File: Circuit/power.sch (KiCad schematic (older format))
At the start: 20 parts, among them Q202 FDN340P, Q203 FDN340P, SW1 ON/OFF, U201 CN3063, U202 MCP6002, U3 LXDC2XQ

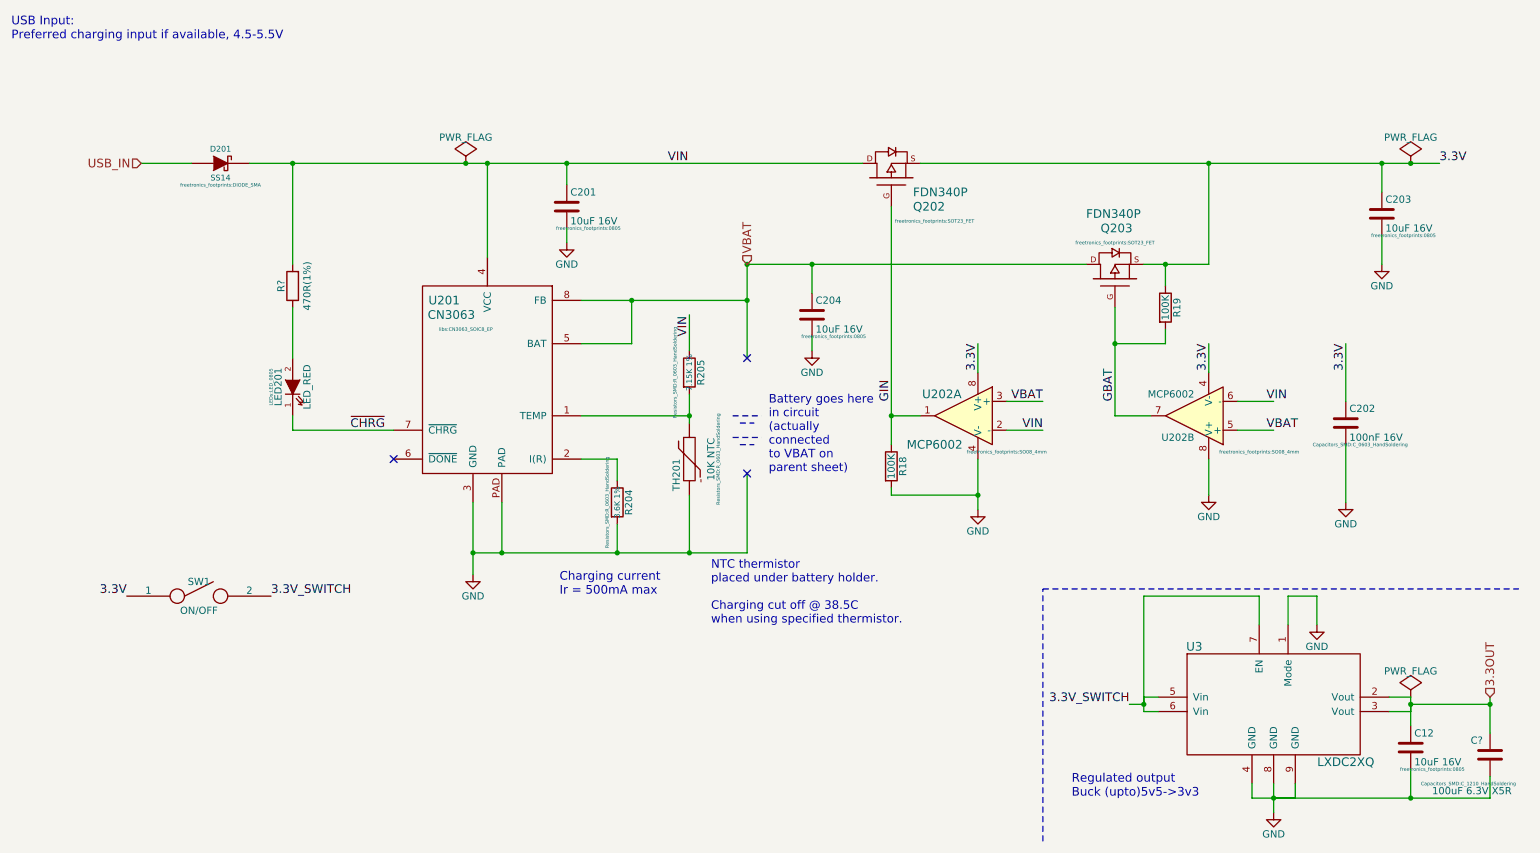
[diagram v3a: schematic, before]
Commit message: Adding LED to 3v3 line.
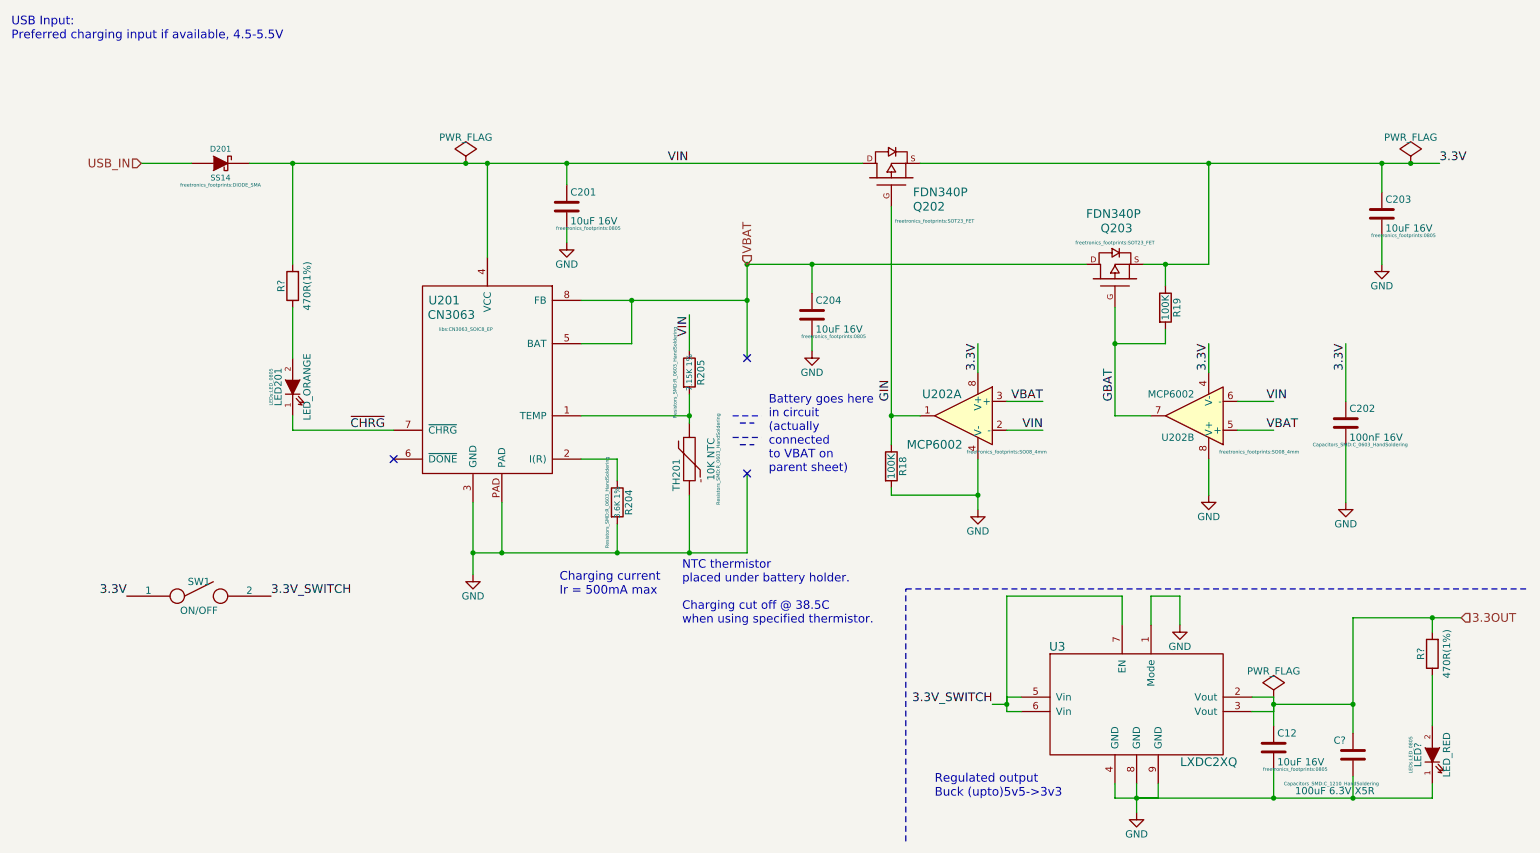
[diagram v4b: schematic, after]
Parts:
- added LED?: LED_RED, LEDs:LED_0805, symbol LED
- added R?: 470R(1%), Resistors_SMD:R_0603_HandSoldering, symbol R
- LED201: value LED_RED -> LED_ORANGE; Digikey PN (none) -> 160-1413-1-ND; Link (none) -> http://www.digikey.com.au/product-detail/en/lite-on-inc/LTS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; Manufacturer PN (none) -> LTST-C170KFKT; Unit Cost (none) -> 0.31
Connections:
- wire segments 74 -> 78
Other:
- moved on the sheet: C12, C?, U3
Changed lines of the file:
@@
 P 2700 3350
 F 0 "LED201" H 2700 3450 50  0000 C CNN
-F 1 "LED_RED" H 2700 3250 50  0000 C CNN
+F 1 "LED_ORANGE" H 2700 3250 50  0000 C CNN
 F 2 "LEDs:LED_0805" H 2700 3500 24  0000 C CNN
 F 3 "" H 2700 3350 60  0000 C CNN
+F 4 "160-1413-1-ND" H 2700 3350 60  0001 C CNN "Digikey PN"
+F 5 "http://www.digikey.com.au/product-detail/en/lite-on-inc/LTST-C170KFKT/160-1413-1-ND/386774" H 2700 3350 60  0001 C CNN "Link"
+F 6 "LTST-C170KFKT" H 2700 3350 60  0001 C CNN "Manufacturer PN"
+F 7 "0.31" H 2700 3350 60  0001 C CNN "Unit Cost"
 	1    2700 3350
 	0    -1   -1   0
@@
 Text Label 6850 3450 1    60   ~ 0
 GIN
-Text HLabel 11000 5500 1    60   Input ~ 0
+Text HLabel 10800 4950 2    60   Input ~ 0
 3.3OUT
 $Comp
@@
 L C C?
 U 1 1 5642CCBE
-P 11000 5900
-F 0 "C?" H 11050 5800 50  0000 L CNN
-F 1 "100uF 6.3V X5R" H 10850 6150 50  0000 L CNN
-F 2 "Capacitors_SMD:C_1210_HandSoldering" H 11150 6100 24  0000 C CNN
-F 3 "" H 11000 5900 60  0000 C CNN
-F 4 "490-7217-1-ND" H 11000 5900 60  0001 C CNN "Digikey PN"
-F 5 "http://www.digikey.com.au/product-detail/en/murata-electronics-north-america/GRM31CR60J107ME39K/490-7217-1-ND/3991203" H 11000 5900 60  0001 C CNN "Link"
-F 6 "GRM31CR60J107ME39K" H 11000 5900 60  0001 C CNN "Manufacturer PN"
-F 7 "0.60" H 11000 5900 60  0001 C CNN "Unit Cost"
-	1    11000 5900
+P 10050 5900
+F 0 "C?" H 10100 5800 50  0000 L CNN
+F 1 "100uF 6.3V X5R" H 9900 6150 50  0000 L CNN
+F 2 "Capacitors_SMD:C_1210_HandSoldering" H 10200 6100 24  0000 C CNN
+F 3 "" H 10050 5900 60  0000 C CNN
+F 4 "490-7217-1-ND" H 10050 5900 60  0001 C CNN "Digikey PN"
+F 5 "http://www.digikey.com.au/product-detail/en/murata-electronics-north-america/GRM31CR60J107ME39K/490-7217-1-ND/3991203" H 10050 5900 60  0001 C CNN "Link"
+F 6 "GRM31CR60J107ME39K" H 10050 5900 60  0001 C CNN "Manufacturer PN"
+F 7 "0.60" H 10050 5900 60  0001 C CNN "Unit Cost"
+	1    10050 5900
 	-1   0    0    1
 $EndComp
@@
 Text Label 5450 3000 1    60   ~ 0
 VIN
-Text Notes 5600 5000 0    59   ~ 0
+Text Notes 5400 5000 0    59   ~ 0
 NTC thermistor\nplaced under battery holder.\n\nCharging cut off @ 38.5C\nwhen using specified thermistor.
 $Comp
@@
 Text Label 10650 1800 0    60   ~ 0
 3.3V
-Text Label 8500 5550 2    60   ~ 0
+Text Label 7550 5550 2    60   ~ 0
 3.3V_SWITCH
 Text Label 2550 4800 0    60   ~ 0
@@
 Text Label 1550 4800 2    60   ~ 0
 3.3V
-Text Notes 8100 6200 0    60   ~ 0
+Text Notes 7150 6200 0    60   ~ 0
 Regulated output\nBuck (upto)5v5->3v3
 Text Label 7450 3050 3    60   ~ 0
@@
 L GND #PWR040
 U 1 1 5812C93A
-P 9500 6300
-F 0 "#PWR040" H 9500 6050 50  0001 C CNN
-F 1 "GND" H 9500 6150 50  0000 C CNN
-F 2 "" H 9500 6300 60  0000 C CNN
-F 3 "" H 9500 6300 60  0000 C CNN
-	1    9500 6300
+P 8550 6300
+F 0 "#PWR040" H 8550 6050 50  0001 C CNN
+F 1 "GND" H 8550 6150 50  0000 C CNN
+F 2 "" H 8550 6300 60  0000 C CNN
+F 3 "" H 8550 6300 60  0000 C CNN
+	1    8550 6300
 	1    0    0    -1
 $EndComp
@@
 L GND #PWR041
 U 1 1 5812E212
-P 9800 5000
-F 0 "#PWR041" H 9800 4750 50  0001 C CNN
-F 1 "GND" H 9800 4850 50  0000 C CNN
-F 2 "" H 9800 5000 60  0000 C CNN
-F 3 "" H 9800 5000 60  0000 C CNN
-	1    9800 5000
+P 8850 5000
+F 0 "#PWR041" H 8850 4750 50  0001 C CNN
+F 1 "GND" H 8850 4850 50  0000 C CNN
+F 2 "" H 8850 5000 60  0000 C CNN
+F 3 "" H 8850 5000 60  0000 C CNN
+	1    8850 5000
 	1    0    0    -1
 $EndComp
@@
 	1650 1800 2000 1800
 Wire Wire Line
-	9350 6200 9650 6200
-Wire Wire Line
-	9350 6100 9350 6200
-Wire Wire Line
-	9500 6100 9500 6300
-Connection ~ 9500 6200
-Wire Wire Line
-	9650 6200 9650 6100
-Wire Wire Line
-	8600 5500 8600 5600
-Wire Wire Line
-	8600 5550 8500 5550
-Wire Wire Line
-	8600 5600 8700 5600
-Connection ~ 8600 5550
-Wire Wire Line
-	8700 5500 8600 5500
-Wire Wire Line
-	10300 5500 10450 5500
-Wire Wire Line
-	10450 5500 10450 5600
-Wire Wire Line
-	10450 5550 11000 5550
-Wire Wire Line
-	10450 5600 10300 5600
-Connection ~ 10450 5550
-Wire Wire Line
-	8600 5550 8600 4800
-Wire Wire Line
-	9400 5000 9400 4800
-Wire Wire Line
-	9400 4800 8600 4800
-Wire Wire Line
-	9600 5000 9600 4800
-Wire Wire Line
-	9600 4800 9800 4800
-Wire Wire Line
-	9800 4800 9800 5000
+	8400 6200 8700 6200
+Wire Wire Line
+	8400 6100 8400 6200
+Wire Wire Line
+	8550 6100 8550 6300
+Connection ~ 8550 6200
+Wire Wire Line
+	8700 6200 8700 6100
+Wire Wire Line
+	7650 5500 7650 5600
+Wire Wire Line
+	7650 5550 7550 5550
+Wire Wire Line
+	7650 5600 7750 5600
+Connection ~ 7650 5550
+Wire Wire Line
+	7750 5500 7650 5500
+Wire Wire Line
+	9350 5500 9500 5500
+Wire Wire Line
+	9500 5500 9500 5600
+Wire Wire Line
+	9500 5550 10050 5550
+Wire Wire Line
+	9500 5600 9350 5600
+Connection ~ 9500 5550
+Wire Wire Line
+	7650 5550 7650 4800
+Wire Wire Line
+	8450 5000 8450 4800
+Wire Wire Line
+	8450 4800 7650 4800
+Wire Wire Line
+	8650 5000 8650 4800
+Wire Wire Line
+	8650 4800 8850 4800
+Wire Wire Line
+	8850 4800 8850 5000
 Wire Notes Line
-	7900 6500 7900 4750
-Wire Notes Line
-	7900 4750 11200 4750
-Wire Wire Line
-	10450 5550 10450 5700
-Wire Wire Line
-	10450 6000 10450 6200
-Wire Wire Line
-	9500 6200 11000 6200
+	6950 6500 6950 4750
+Wire Wire Line
+	9500 5550 9500 5700
+Wire Wire Line
+	9500 6000 9500 6200
+Wire Wire Line
+	8550 6200 10600 6200
 $Comp
 L LXDC2XQ U3
 U 1 1 581FF216
-P 9500 5550
-F 0 "U3" H 8950 5950 60  0000 C CNN
-F 1 "LXDC2XQ" H 10000 5150 60  0000 C CNN
-F 2 "" H 8850 5850 60  0001 C CNN
-F 3 "http://power.murata.com/data/power/LXDC2XQ_Series_datasheet.pdf" H 8950 5950 60  0001 C CNN
-F 4 "http://www.digikey.com.au/product-detail/en/murata-electronics-north-america/LXDC2XQ33A-254/490-12573-1-ND/5797558" H 9050 6050 60  0001 C CNN "Digikey URL"
-F 5 "1.55" H 9150 6150 60  0001 C CNN "Unit cost"
-F 6 "490-12573-1-ND" H 9250 6250 60  0001 C CNN "Digikey PN"
-	1    9500 5550
+P 8550 5550
+F 0 "U3" H 8000 5950 60  0000 C CNN
+F 1 "LXDC2XQ" H 9050 5150 60  0000 C CNN
+F 2 "" H 7900 5850 60  0001 C CNN
+F 3 "http://power.murata.com/data/power/LXDC2XQ_Series_datasheet.pdf" H 8000 5950 60  0001 C CNN
+F 4 "http://www.digikey.com.au/product-detail/en/murata-electronics-north-america/LXDC2XQ33A-254/490-12573-1-ND/5797558" H 8100 6050 60  0001 C CNN "Digikey URL"
+F 5 "1.55" H 8200 6150 60  0001 C CNN "Unit cost"
+F 6 "490-12573-1-ND" H 8300 6250 60  0001 C CNN "Digikey PN"
+	1    8550 5550
 	1    0    0    -1
 $EndComp
@@
 $EndComp
 Wire Wire Line
-	11000 5500 11000 5750
-Connection ~ 11000 5550
-Wire Wire Line
-	11000 6200 11000 6050
-Connection ~ 10450 6200
+	10050 4950 10050 5750
+Connection ~ 10050 5550
+Wire Wire Line
+	10050 6200 10050 6050
+Connection ~ 9500 6200
 $Comp
 L PWR_FLAG #FLG?
 U 1 1 58217320
-P 10450 5500
-F 0 "#FLG?" H 10450 5595 50  0001 C CNN
-F 1 "PWR_FLAG" H 10450 5680 50  0000 C CNN
-F 2 "" H 10450 5500 60  0000 C CNN
-F 3 "" H 10450 5500 60  0000 C CNN
-	1    10450 5500
+P 9500 5500
+F 0 "#FLG?" H 9500 5595 50  0001 C CNN
+F 1 "PWR_FLAG" H 9500 5680 50  0000 C CNN
+F 2 "" H 9500 5500 60  0000 C CNN
+F 3 "" H 9500 5500 60  0000 C CNN
+	1    9500 5500
 	1    0    0    -1
 $EndComp
@@
 L C C12
 U 1 1 58218A3F
-P 10450 5850
-F 0 "C12" H 10475 5950 50  0000 L CNN
-F 1 "10uF 16V" H 10475 5750 50  0000 L CNN
-F 2 "freetronics_footprints:0805" H 10600 5700 24  0000 C CNN
-F 3 "" H 10450 5850 60  0000 C CNN
-F 4 "1276-2399-1-ND" H 10450 5850 60  0001 C CNN "Digikey PN"
-F 5 "http://www.digikey.com.au/product-detail/en/samsung-electro-mechanics-america-inc/CL21A106KOCLRNC/1276-2399-1-ND/3890485" H 10450 5850 60  0001 C CNN "Link"
-F 6 "CL21A106KOCLRNC" H 10450 5850 60  0001 C CNN "Manufacturer PN"
-F 7 "0.18" H 10450 5850 60  0001 C CNN "Unit Cost"
-	1    10450 5850
-	1    0    0    -1
-$EndComp
+P 9500 5850
+F 0 "C12" H 9525 5950 50  0000 L CNN
+F 1 "10uF 16V" H 9525 5750 50  0000 L CNN
+F 2 "freetronics_footprints:0805" H 9650 5700 24  0000 C CNN
+F 3 "" H 9500 5850 60  0000 C CNN
+F 4 "1276-2399-1-ND" H 9500 5850 60  0001 C CNN "Digikey PN"
+F 5 "http://www.digikey.com.au/product-detail/en/samsung-electro-mechanics-america-inc/CL21A106KOCLRNC/1276-2399-1-ND/3890485" H 9500 5850 60  0001 C CNN "Link"
+F 6 "CL21A106KOCLRNC" H 9500 5850 60  0001 C CNN "Manufacturer PN"
+F 7 "0.18" H 9500 5850 60  0001 C CNN "Unit Cost"
+	1    9500 5850
+	1    0    0    -1
+$EndComp
+$Comp
+L LED LED?
+U 1 1 5822B84F
+P 10600 5900
+F 0 "LED?" H 10600 6000 50  0000 C CNN
+F 1 "LED_RED" H 10600 5800 50  0000 C CNN
+F 2 "LEDs:LED_0805" H 10600 6050 24  0000 C CNN
+F 3 "" H 10600 5900 60  0000 C CNN
+F 4 "732-4984-1-ND" H 10600 5900 60  0001 C CNN "Digikey PN"
+F 5 "http://www.digikey.com.au/product-detail/en/wurth-electronics-inc/150080RS75000/732-4984-1-ND/4489916" H 10600 5900 60  0001 C CNN "Link"
+F 6 "150080RS75000" H 10600 5900 60  0001 C CNN "Manufacturer PN"
+F 7 "0.29" H 10600 5900 60  0001 C CNN "Unit Cost"
+	1    10600 5900
+	0    -1   -1   0
+$EndComp
+Wire Wire Line
+	10600 5350 10600 5700
+$Comp
+L R R?
+U 1 1 5822B85B
+P 10600 5200
+F 0 "R?" V 10680 5200 50  0000 C CNN
+F 1 "470R(1%)" V 10500 5200 50  0000 C CNN
+F 2 "Resistors_SMD:R_0603_HandSoldering" V 10530 5200 50  0001 C CNN
+F 3 "" H 10600 5200 50  0000 C CNN
+F 4 "311-470HRCT-ND" V 10600 5200 60  0001 C CNN "Digikey PN"
+F 5 "http://www.digikey.com.au/product-detail/en/yageo/RC0603FR-07470RL/311-470HRCT-ND/730203" V 10600 5200 60  0001 C CNN "Link"
+F 6 "RC0603FR-07470RL" V 10600 5200 60  0001 C CNN "Manufacturer PN"
+F 7 "0.10" V 10600 5200 60  0001 C CNN "Unit Cost"
+	1    10600 5200
+	-1   0    0    1
+$EndComp
+Wire Wire Line
+	10600 6200 10600 6100
+Connection ~ 10050 6200
+Wire Wire Line
+	10050 4950 10800 4950
+Wire Wire Line
+	10600 5050 10600 4950
+Connection ~ 10600 4950
+Wire Notes Line
+	6950 4750 11250 4750
 $EndSCHEMATC

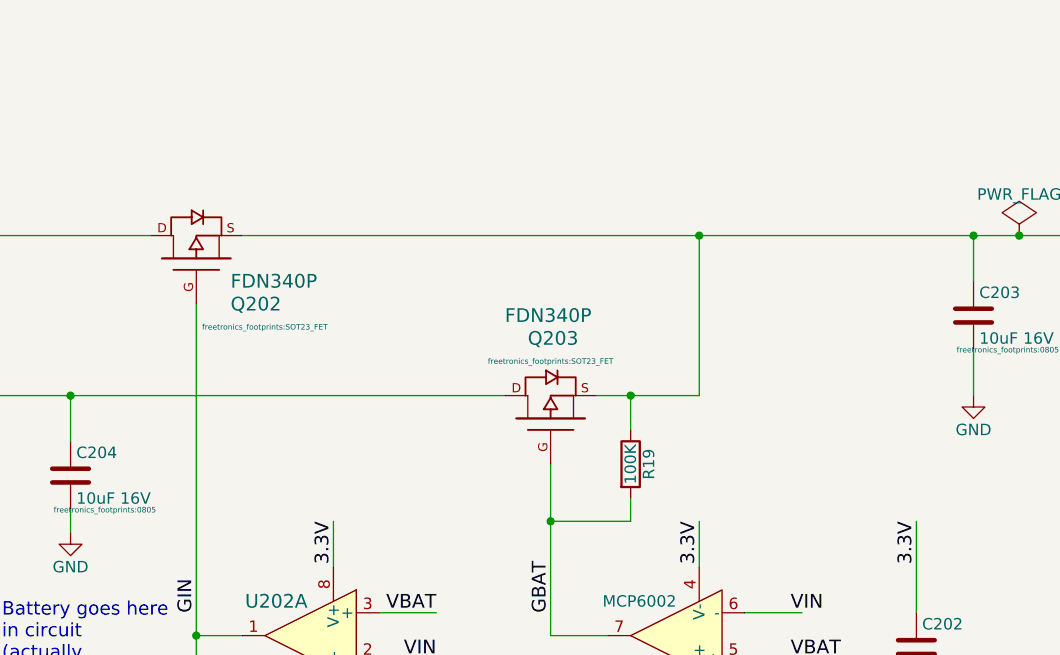
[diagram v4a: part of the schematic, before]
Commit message: BOM. Some passives & transistors. Nearly done.
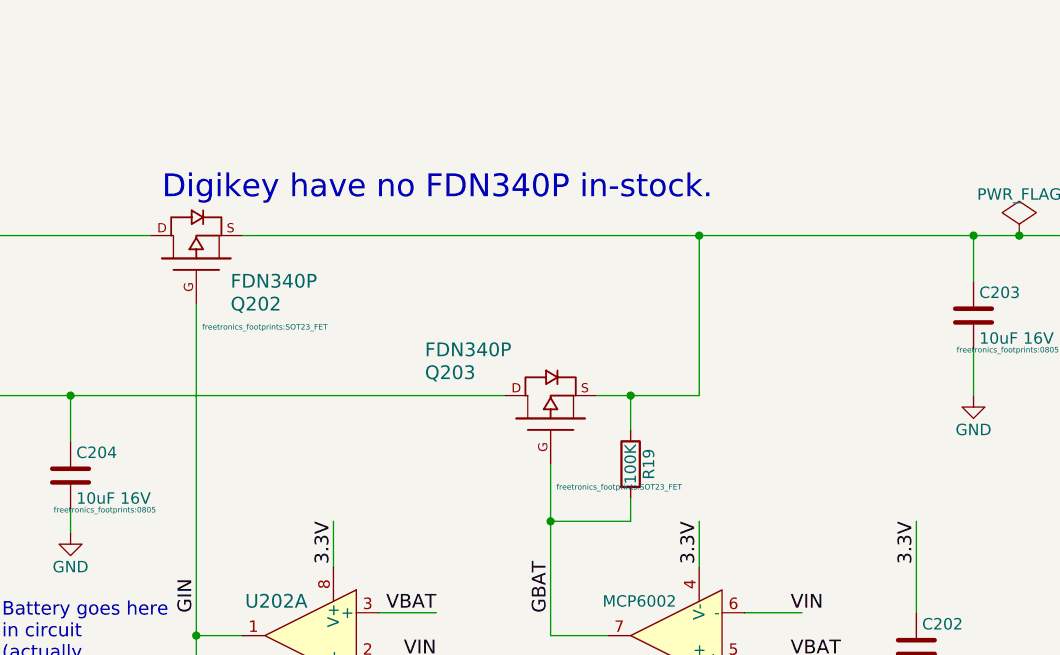
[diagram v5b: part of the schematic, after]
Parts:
- Q202, Q203: Digikey PN (none) -> FDN340PCT-ND; Link (none) -> http://www.digikey.com.au/product-detail/en/fairchild-semic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; Manufacturer PN (none) -> FDN340P; Unit Cost (none) -> 0.39
- R18, R19: Digikey PN (none) -> 311-100KGRCT-ND; Link (none) -> http://www.digikey.com.au/product-detail/en/yageo/RC0603JR-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; Manufacturer PN (none) -> RC0603JR-07100KL; Unit Cost (none) -> 0.10
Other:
- note added: "Digikey have no FDN340P in-stock."
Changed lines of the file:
@@
 F 2 "freetronics_footprints:SOT23_FET" V 6550 1600 24  0000 C CNN
 F 3 "" H 6850 1900 60  0000 C CNN
+F 4 "FDN340PCT-ND" V 6850 1900 60  0001 C CNN "Digikey PN"
+F 5 "http://www.digikey.com.au/product-detail/en/fairchild-semiconductor/FDN340P/FDN340PCT-ND/965604" V 6850 1900 60  0001 C CNN "Link"
+F 6 "FDN340P" V 6850 1900 60  0001 C CNN "Manufacturer PN"
+F 7 "0.39" V 6850 1900 60  0001 C CNN "Unit Cost"
 	1    6850 1900
 	0    -1   -1   0
@@
 	1    7450 4200
 	-1   0    0    -1
-$EndComp
-$Comp
-L MOSFET_P Q203
-U 1 1 5641832A
-P 8400 2600
-F 0 "Q203" V 8750 2700 60  0000 R CNN
-F 1 "FDN340P" V 8850 2800 60  0000 R CNN
-F 2 "freetronics_footprints:SOT23_FET" V 8650 2600 24  0000 C CNN
-F 3 "" H 8400 2600 60  0000 C CNN
-	1    8400 2600
-	0    -1   -1   0
 $EndComp
 Text Label 8400 3450 1    60   ~ 0
@@
 F 2 "Resistors_SMD:R_0603_HandSoldering" V 6780 3900 50  0001 C CNN
 F 3 "" H 6850 3900 50  0000 C CNN
+F 4 "311-100KGRCT-ND" V 6850 3900 60  0001 C CNN "Digikey PN"
+F 5 "http://www.digikey.com.au/product-detail/en/yageo/RC0603JR-07100KL/311-100KGRCT-ND/729645" V 6850 3900 60  0001 C CNN "Link"
+F 6 "RC0603JR-07100KL" V 6850 3900 60  0001 C CNN "Manufacturer PN"
+F 7 "0.10" V 6850 3900 60  0001 C CNN "Unit Cost"
 	1    6850 3900
-	1    0    0    -1
-$EndComp
-$Comp
-L R R19
-U 1 1 56EBECD6
-P 8750 2800
-F 0 "R19" V 8830 2800 50  0000 C CNN
-F 1 "100K" V 8750 2800 50  0000 C CNN
-F 2 "Resistors_SMD:R_0603_HandSoldering" V 8680 2800 50  0001 C CNN
-F 3 "" H 8750 2800 50  0000 C CNN
-	1    8750 2800
 	1    0    0    -1
 $EndComp
@@
 Wire Notes Line
 	6950 4750 11250 4750
+Text Notes 6700 1650 0    100  ~ 0
+Digikey have no FDN340P in-stock.
+$Comp
+L MOSFET_P Q203
+U 1 1 5822C664
+P 8400 2600
+F 0 "Q203" V 8600 3150 60  0000 R CNN
+F 1 "FDN340P" V 8700 3150 60  0000 R CNN
+F 2 "freetronics_footprints:SOT23_FET" V 8100 2300 24  0000 C CNN
+F 3 "" H 8400 2600 60  0000 C CNN
+F 4 "FDN340PCT-ND" V 8400 2600 60  0001 C CNN "Digikey PN"
+F 5 "http://www.digikey.com.au/product-detail/en/fairchild-semiconductor/FDN340P/FDN340PCT-ND/965604" V 8400 2600 60  0001 C CNN "Link"
+F 6 "FDN340P" V 8400 2600 60  0001 C CNN "Manufacturer PN"
+F 7 "0.39" V 8400 2600 60  0001 C CNN "Unit Cost"
+	1    8400 2600
+	0    -1   -1   0
+$EndComp
+$Comp
+L R R19
+U 1 1 5822E061
+P 8750 2800
+F 0 "R19" V 8830 2800 50  0000 C CNN
+F 1 "100K" V 8750 2800 50  0000 C CNN
+F 2 "Resistors_SMD:R_0603_HandSoldering" V 8680 2800 50  0001 C CNN
+F 3 "" H 8750 2800 50  0000 C CNN
+F 4 "311-100KGRCT-ND" V 8750 2800 60  0001 C CNN "Digikey PN"
+F 5 "http://www.digikey.com.au/product-detail/en/yageo/RC0603JR-07100KL/311-100KGRCT-ND/729645" V 8750 2800 60  0001 C CNN "Link"
+F 6 "RC0603JR-07100KL" V 8750 2800 60  0001 C CNN "Manufacturer PN"
+F 7 "0.10" V 8750 2800 60  0001 C CNN "Unit Cost"
+	1    8750 2800
+	1    0    0    -1
+$EndComp
 $EndSCHEMATC

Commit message: Sensor ICs BOM information.
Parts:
- U201: Non-Digikey (none) -> 1
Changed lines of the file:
@@
 F 2 "libs:CN3063_SOIC8_EP" H 3900 3550 24  0000 C CNN
 F 3 "" H 3800 2900 60  0000 C CNN
+F 4 "1" H 4050 3250 60  0001 C CNN "Non-Digikey"
 	1    4050 3250
 	1    0    0    -1
